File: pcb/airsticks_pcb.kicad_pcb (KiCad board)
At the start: 2 copper layers, 48.7 x 22.5 mm, 69 parts, among them J1 USB_C_Receptacle_USB2.0, J2 STM_LINK, J3 USB_SERIAL_TTL, J4 I2C, J5 AudioJack3, U1 STM32G441KBT6, U4 PAM8302AAS, U5 TC1262-33

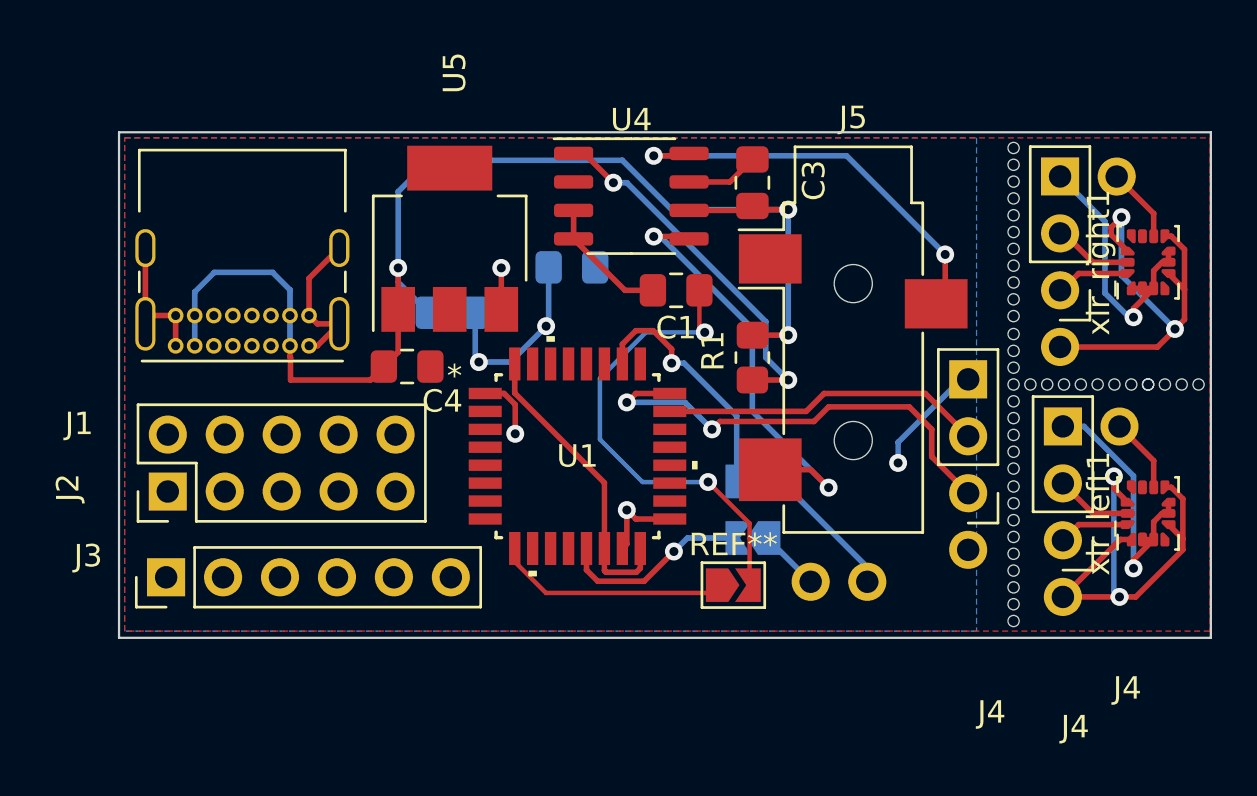
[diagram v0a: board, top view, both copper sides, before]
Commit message: updated PCB to reflect changes we made. NOTE: still need to make the boot0 change, as it is still currently floating
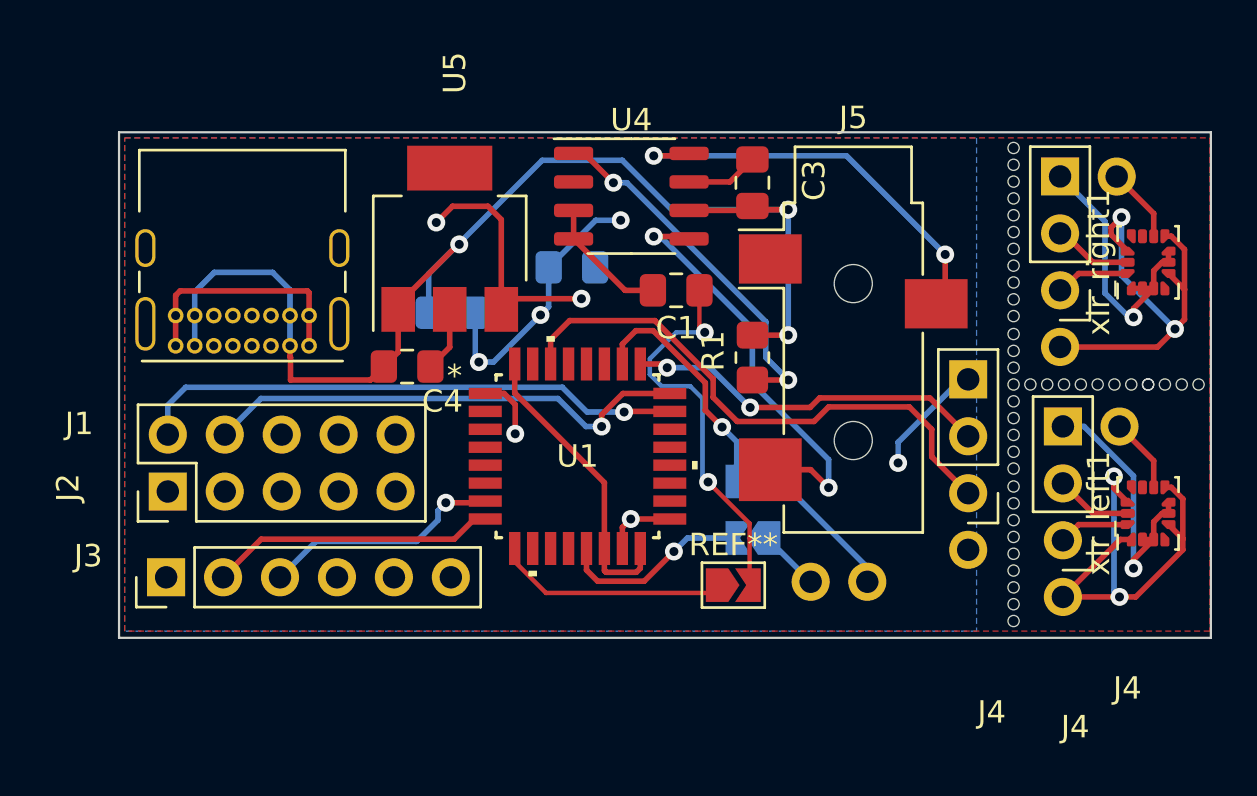
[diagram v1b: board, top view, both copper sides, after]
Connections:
- J1 pad S1: GND -> (no net)
- J2 pad 2: /SWCLK -> /SWDIO
- J2 pad 4: /SWDIO -> /SWCLK
- J4 pad 1: /I2C1_SDA -> /I2C_SDA (x3)
- J4 pad 2: /I2C1_SLC -> /I2C_SCL (x2)
- U1 pad 23: /I2C1_SLC -> /SWDIO
- U1 pad 24: /I2C1_SDA -> /SWCLK
- U1 pad 25: unconnected-(U1-Pad25) -> /I2C_SCL
- U1 pad 30: unconnected-(U1-Pad30) -> /I2C_SDA
- U1 pad 7: unconnected-(U1-Pad7) -> /TX
- U1 pad 8: unconnected-(U1-Pad8) -> /RX
- xlr_left1 pad 13: /I2C1_SLC -> /I2C_SCL
- xlr_left1 pad 14: /I2C1_SDA -> /I2C_SDA
- xlr_right1 pad 13: /I2C1_SLC -> /I2C_SCL
- xlr_right1 pad 14: /I2C1_SDA -> /I2C_SDA
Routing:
- net /I2C_SDA: track 0.00 -> 31.3 mm
- net /I2C1_SDA: track 26.9 -> 0.00 mm, vias 2 -> 0
- net /SWDIO: track 0.00 -> 24.5 mm, vias 0 -> 1
- net /I2C_SCL: track 0.00 -> 23.2 mm, vias 0 -> 2
- net /SWCLK: track 0.00 -> 22.0 mm, vias 0 -> 1
- net /I2C1_SLC: track 21.3 -> 0.00 mm
- net /RX: track 0.00 -> 12.8 mm
- net /TX: track 0.00 -> 10.8 mm, vias 0 -> 1
- net +3V3: track 48.9 -> 57.6 mm, vias 7 -> 8
- net GND: track 68.3 -> 72.4 mm, vias 5 -> 6
- net /AUDIO+: track 31.5 -> 27.9 mm
- net +5V: track 57.1 -> 55.2 mm
